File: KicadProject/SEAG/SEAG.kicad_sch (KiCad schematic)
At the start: 0 parts

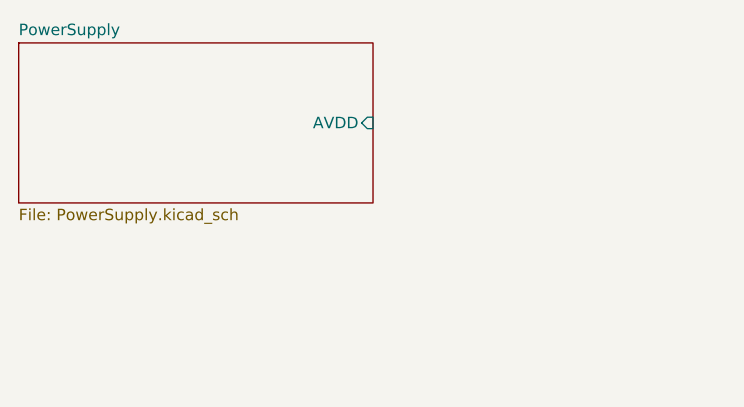
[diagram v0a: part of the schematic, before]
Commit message: Added power supply and serial link header to PCB schematic
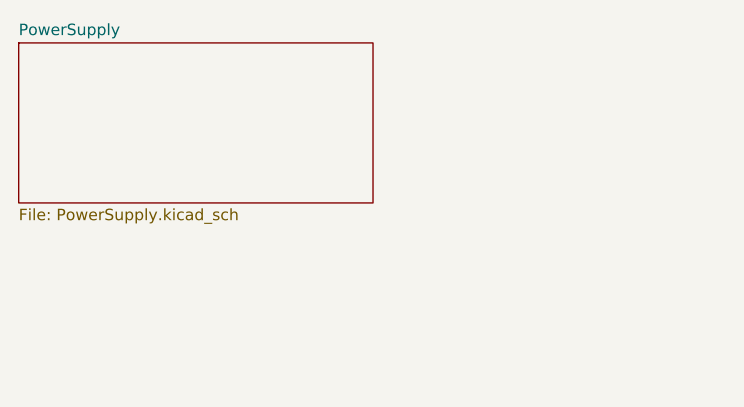
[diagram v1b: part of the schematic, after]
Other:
- sheet PowerSupply ports: added none; removed AVDD
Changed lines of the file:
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@@
       (effects (font (size 1.27 1.27)) (justify left top))
-    )
-    (pin "AVDD" input (at 61.595 27.305 0)
-      (effects (font (size 1.27 1.27)) (justify right))
     )
     (instances

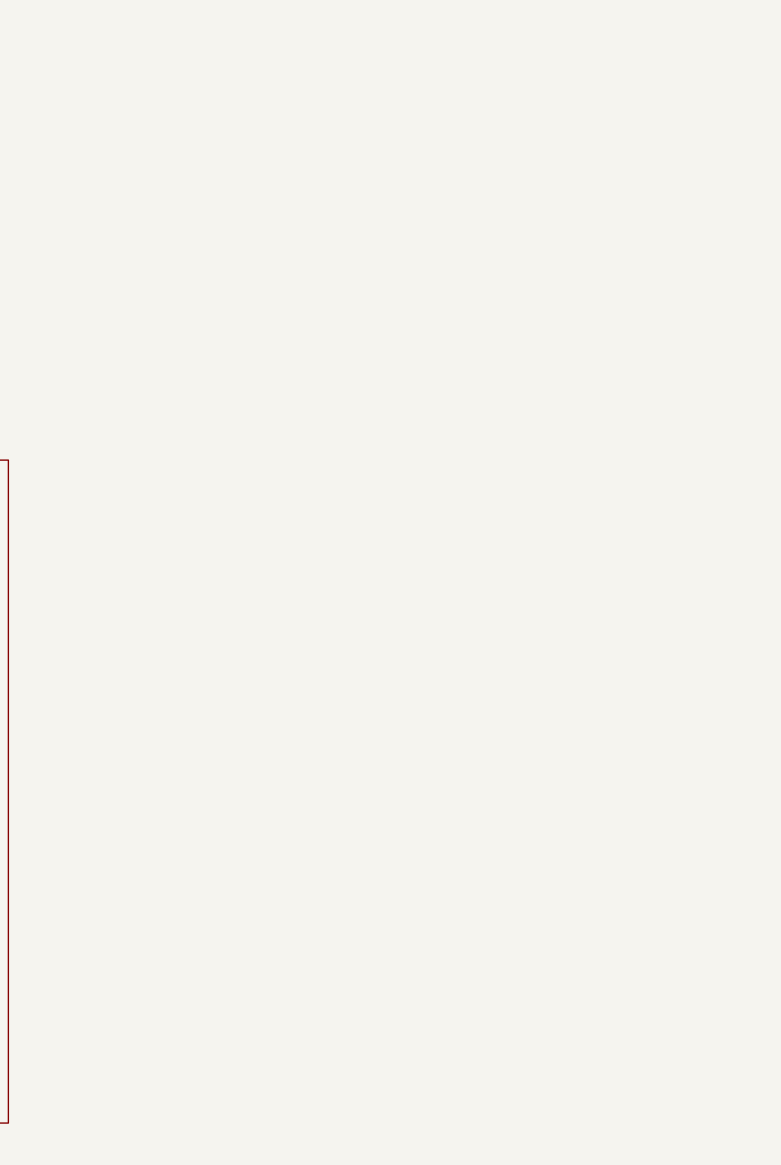
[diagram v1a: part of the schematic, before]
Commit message: Added 'AudioFiltering' and 'Codec' sheets to PCB schematic, started PCB layout with decouple caps and MCU. The codec in sheet 'Codec' is wrong, placed for testing
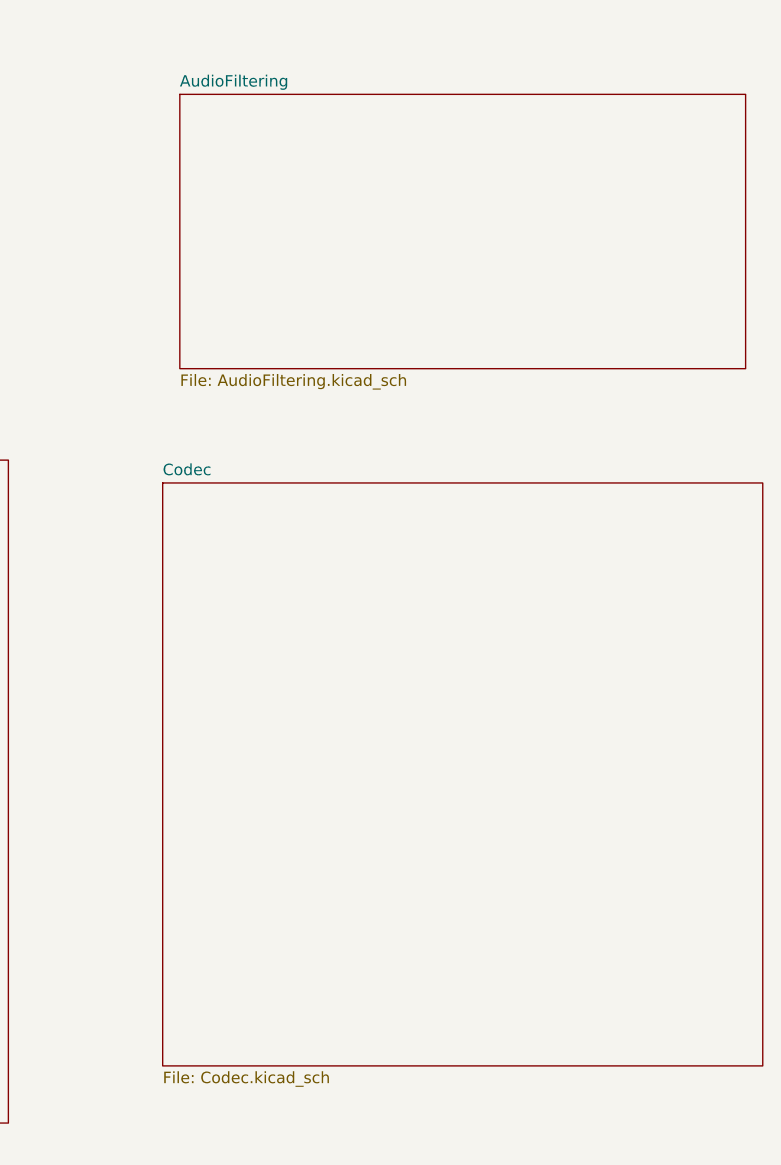
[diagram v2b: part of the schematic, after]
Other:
- added sheet AudioFiltering (AudioFiltering.kicad_sch)
- added sheet Codec (Codec.kicad_sch)
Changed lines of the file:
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@@
 (kicad_sch (version 20230121) (generator eeschema)
   (paper "A4")
+  (sheet (at 188.595 24.13) (size 62.865 30.48) (fields_autoplaced)
+    (stroke (width 0.1524) (type solid))
+    (fill (color 0 0 0 0.0000))
+    (property "Sheetname" "AudioFiltering" (at 188.595 23.4184 0)
+      (effects (font (size 1.27 1.27)) (justify left bottom))
+    )
+    (property "Sheetfile" "AudioFiltering.kicad_sch" (at 188.595 55.1946 0)
+      (effects (font (size 1.27 1.27)) (justify left top))
+    )
+    (instances
+      (project "SEAG"
+        (path "/37e7da6e-dab5-4e62-b28a-754ec4806405" (page "4"))
+      )
+    )
+  )
   (sheet (at 22.225 18.415) (size 39.37 17.78) (fields_autoplaced)
     (stroke (width 0.1524) (type solid))
@@
       )
     )
+  )
+  (sheet (at 186.69 67.31) (size 66.675 64.77) (fields_autoplaced)
+    (stroke (width 0.1524) (type solid))
+    (fill (color 0 0 0 0.0000))
+    (property "Sheetname" "Codec" (at 186.69 66.5984 0)
+      (effects (font (size 1.27 1.27)) (justify left bottom))
+    )
+    (property "Sheetfile" "Codec.kicad_sch" (at 186.69 132.6646 0)
+      (effects (font (size 1.27 1.27)) (justify left top))
+    )
+    (instances
+      (project "SEAG"
+        (path "/37e7da6e-dab5-4e62-b28a-754ec4806405" (page "5"))
+      )
+    )

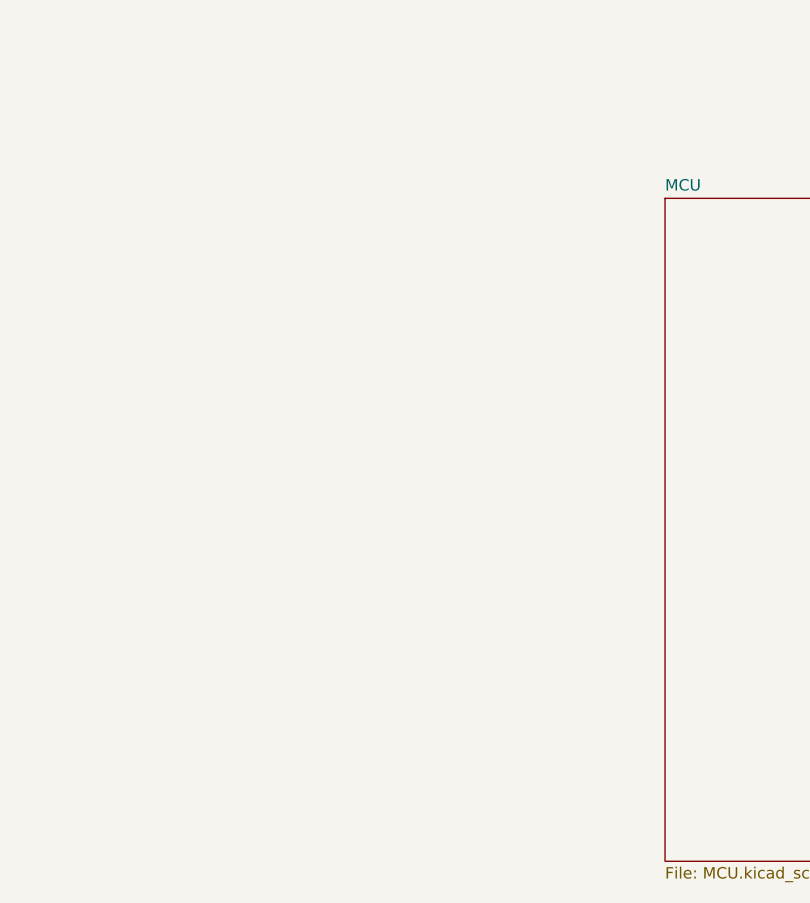
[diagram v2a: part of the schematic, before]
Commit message: Finished PCB, stil uncertain about couple things
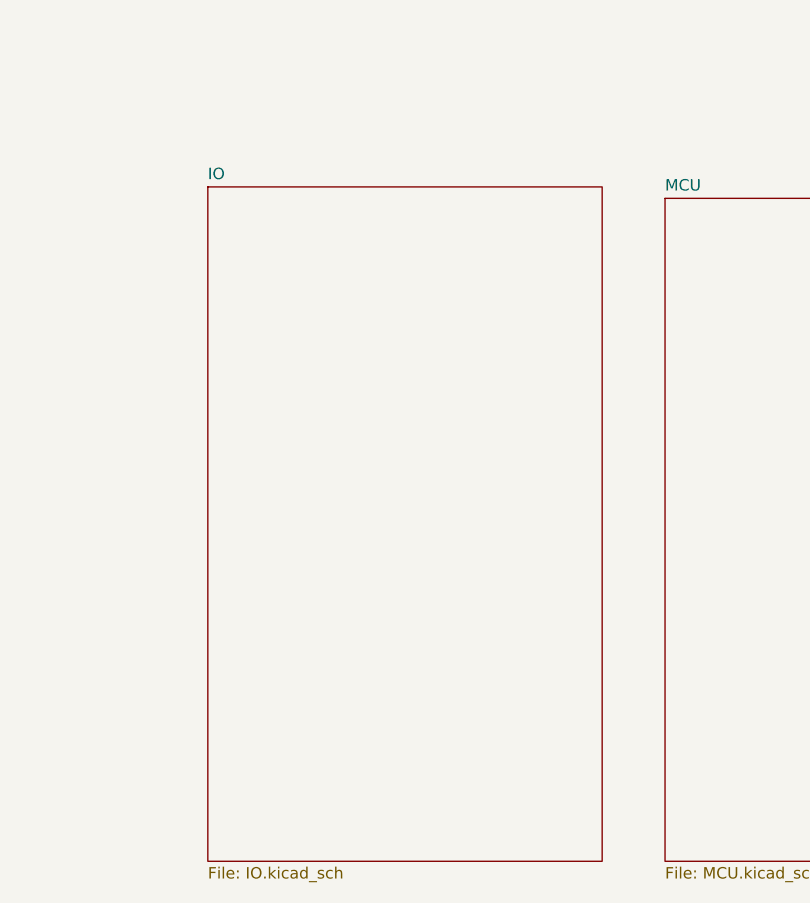
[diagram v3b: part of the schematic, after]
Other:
- added sheet IO (IO.kicad_sch)
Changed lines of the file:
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@@
+    )
+  )
+  (sheet (at 56.515 63.5) (size 43.815 74.93) (fields_autoplaced)
+    (stroke (width 0.1524) (type solid))
+    (fill (color 0 0 0 0.0000))
+    (property "Sheetname" "IO" (at 56.515 62.7884 0)
+      (effects (font (size 1.27 1.27)) (justify left bottom))
+    )
+    (property "Sheetfile" "IO.kicad_sch" (at 56.515 139.0146 0)
+      (effects (font (size 1.27 1.27)) (justify left top))
+    )
+    (instances
+      (project "SEAG"
+        (path "/37e7da6e-dab5-4e62-b28a-754ec4806405" (page "6"))
+      )
     )
   )

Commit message: Slight PCB changes
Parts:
- added H1, H2, H3, H4: MountingHole, MountingHole:MountingHole_3mm, symbol Mechanical:MountingHole
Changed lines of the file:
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@@
 (kicad_sch (version 20230121) (generator eeschema)
   (paper "A4")
+  (symbol (lib_id "Mechanical:MountingHole") (at 81.915 31.115 0) (unit 1)
+    (in_bom yes) (on_board yes) (dnp no) (fields_autoplaced)
+    (property "Reference" "H3" (at 85.09 29.845 0)
+      (effects (font (size 1.27 1.27)) (justify left))
+    )
+    (property "Value" "MountingHole" (at 85.09 32.385 0)
+      (effects (font (size 1.27 1.27)) (justify left))
+    )
+    (property "Footprint" "MountingHole:MountingHole_3mm" (at 81.915 31.115 0)
+      (effects (font (size 1.27 1.27)) hide)
+    )
+    (property "Datasheet" "~" (at 81.915 31.115 0)
+      (effects (font (size 1.27 1.27)) hide)
+    )
+    (instances
+      (project "SEAG"
+        (path "/37e7da6e-dab5-4e62-b28a-754ec4806405"
+          (reference "H3") (unit 1)
+        )
+      )
+    )
+  )
+  (symbol (lib_id "Mechanical:MountingHole") (at 81.915 22.225 0) (unit 1)
+    (in_bom yes) (on_board yes) (dnp no) (fields_autoplaced)
+    (property "Reference" "H1" (at 85.09 20.955 0)
+      (effects (font (size 1.27 1.27)) (justify left))
+    )
+    (property "Value" "MountingHole" (at 85.09 23.495 0)
+      (effects (font (size 1.27 1.27)) (justify left))
+    )
+    (property "Footprint" "MountingHole:MountingHole_3mm" (at 81.915 22.225 0)
+      (effects (font (size 1.27 1.27)) hide)
+    )
+    (property "Datasheet" "~" (at 81.915 22.225 0)
+      (effects (font (size 1.27 1.27)) hide)
+    )
+    (instances
+      (project "SEAG"
+        (path "/37e7da6e-dab5-4e62-b28a-754ec4806405"
+          (reference "H1") (unit 1)
+        )
+      )
+    )
+  )
+  (symbol (lib_id "Mechanical:MountingHole") (at 81.915 35.56 0) (unit 1)
+    (in_bom yes) (on_board yes) (dnp no) (fields_autoplaced)
+    (property "Reference" "H4" (at 85.09 34.29 0)
+      (effects (font (size 1.27 1.27)) (justify left))
+    )
+    (property "Value" "MountingHole" (at 85.09 36.83 0)
+      (effects (font (size 1.27 1.27)) (justify left))
+    )
+    (property "Footprint" "MountingHole:MountingHole_3mm" (at 81.915 35.56 0)
+      (effects (font (size 1.27 1.27)) hide)
+    )
+    (property "Datasheet" "~" (at 81.915 35.56 0)
+      (effects (font (size 1.27 1.27)) hide)
+    )
+    (instances
+      (project "SEAG"
+        (path "/37e7da6e-dab5-4e62-b28a-754ec4806405"
+          (reference "H4") (unit 1)
+        )
+      )
+    )
+  )
+  (symbol (lib_id "Mechanical:MountingHole") (at 81.915 26.67 0) (unit 1)
+    (in_bom yes) (on_board yes) (dnp no) (fields_autoplaced)
+    (property "Reference" "H2" (at 85.09 25.4 0)
+      (effects (font (size 1.27 1.27)) (justify left))
+    )
+    (property "Value" "MountingHole" (at 85.09 27.94 0)
+      (effects (font (size 1.27 1.27)) (justify left))
+    )
+    (property "Footprint" "MountingHole:MountingHole_3mm" (at 81.915 26.67 0)
+      (effects (font (size 1.27 1.27)) hide)
+    )
+    (property "Datasheet" "~" (at 81.915 26.67 0)
+      (effects (font (size 1.27 1.27)) hide)
+    )
+    (instances
+      (project "SEAG"
+        (path "/37e7da6e-dab5-4e62-b28a-754ec4806405"
+          (reference "H2") (unit 1)
+        )
+      )
+    )
+  )
   (sheet (at 188.595 24.13) (size 62.865 30.48) (fields_autoplaced)
     (stroke (width 0.1524) (type solid))
